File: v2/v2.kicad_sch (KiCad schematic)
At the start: 63 parts, among them SW1 SW_Push, SW10 SW_Push, SW11 SW_Push, SW12 SW_Push, SW13 SW_Push, SW14 SW_Push, SW15 SW_Push, SW16 SW_Push, SW17 SW_Push, SW18 SW_Push, SW19 SW_Push, SW2 SW_Push, SW20 SW_Push, SW21 SW_Push, SW22 SW_Push, SW23 SW_Push, SW24 SW_Push, SW25 SW_Push, SW26 SW_Push, SW27 SW_Push, SW28 SW_Push, SW29 SW_Push, SW3 SW_Push, SW30 SW_Push, SW31 SW_Push, SW4 SW_Push, SW5 SW_Push, SW6 SW_Push, SW7 SW_Push, SW8 SW_Push, SW9 SW_Push, U1 Pico

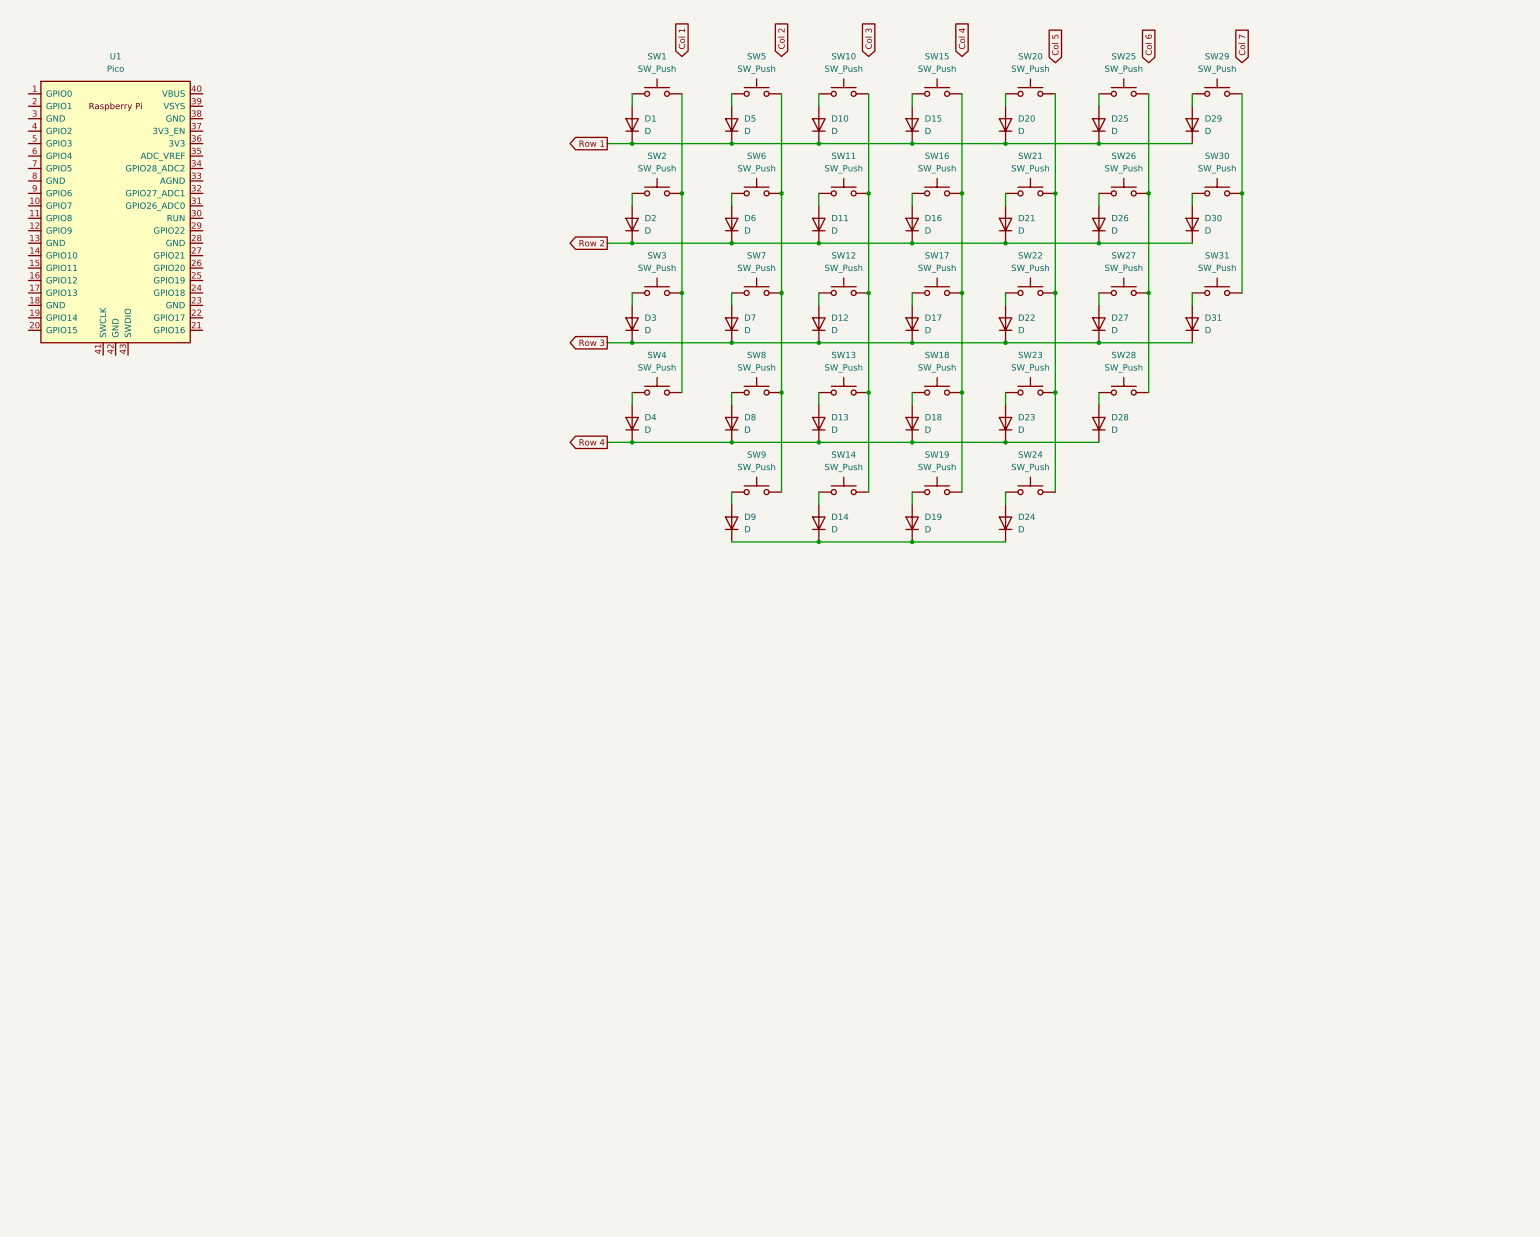
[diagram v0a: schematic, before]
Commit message: get the right footprints finally
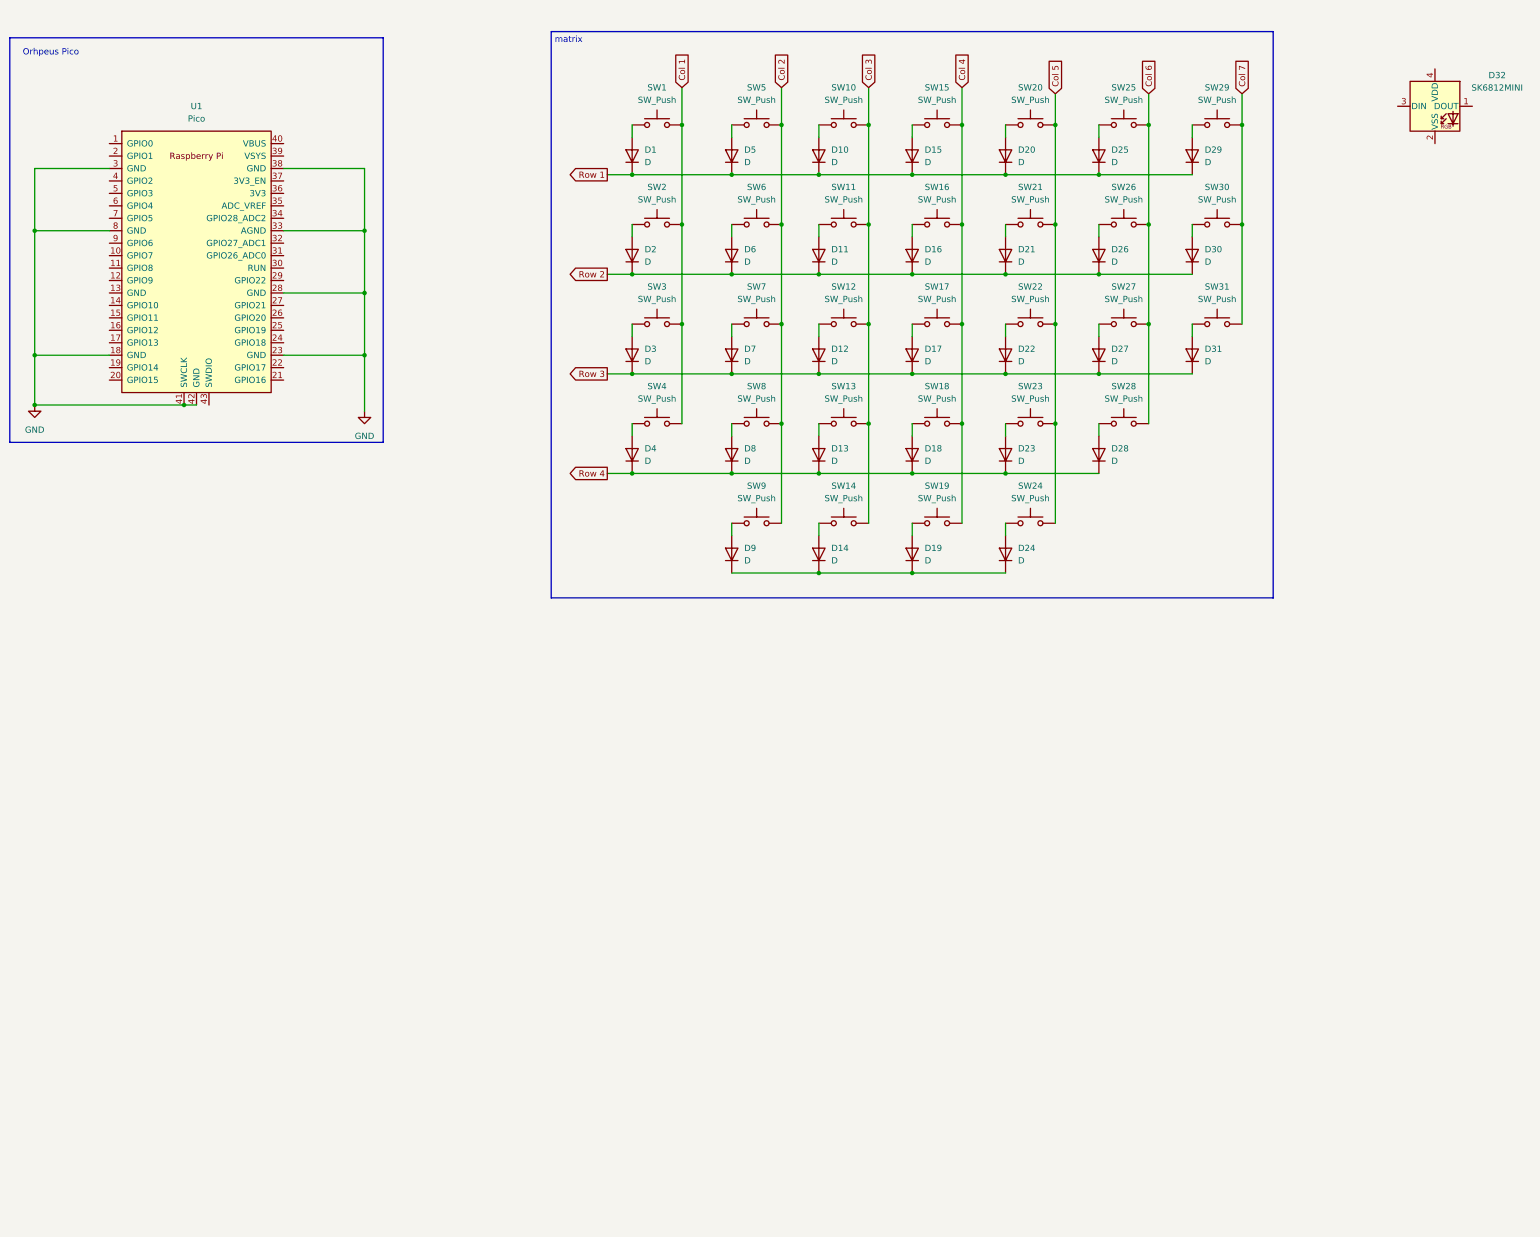
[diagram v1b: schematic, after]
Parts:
- added D32: SK6812MINI, reversible-kicad-footprints:MX-1U-SK6812Mini-E, symbol LED:SK6812MINI
- SW1, SW10, SW11, SW12, SW13, SW14, SW15, SW16, SW17, SW18, SW19, SW2, SW20, SW21, SW22, SW23, SW24, SW25, SW26, SW27, SW28, SW29, SW3, SW30, SW31, SW4, SW5, SW6, SW7, SW8, SW9: footprint (none) -> reversible-kicad-footprints:MX-1U-Hotswap
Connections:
- net Col 1: now also SW1.2, SW2.2, SW3.2, SW4.2
- net Col 2: now also SW5.2, SW6.2, SW7.2, SW8.2, SW9.2
- net Col 3: now also SW10.2, SW11.2, SW12.2, SW13.2, SW14.2
- net Col 4: now also SW15.2, SW16.2, SW17.2, SW18.2, SW19.2
- net Col 5: now also SW20.2, SW21.2, SW22.2, SW23.2, SW24.2
- net Col 6: now also SW25.2, SW26.2, SW27.2, SW28.2
- net Col 7: now also SW29.2, SW30.2, SW31.2
- net GND: now reaches U1.18 (GND)
- net GND: now also U1.23 (GND), U1.28 (GND), U1.3 (GND), U1.33 (AGND), U1.38 (GND), U1.41 (SWCLK), U1.42 (GND), U1.8 (GND)
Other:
- note added: "Orhpeus Pico"
- note added: "matrix"
- moved on the sheet: D1, D10, D11, D12, D13, D14, D15, D16, D17, D18, D19, D2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

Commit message: started adding backlighting
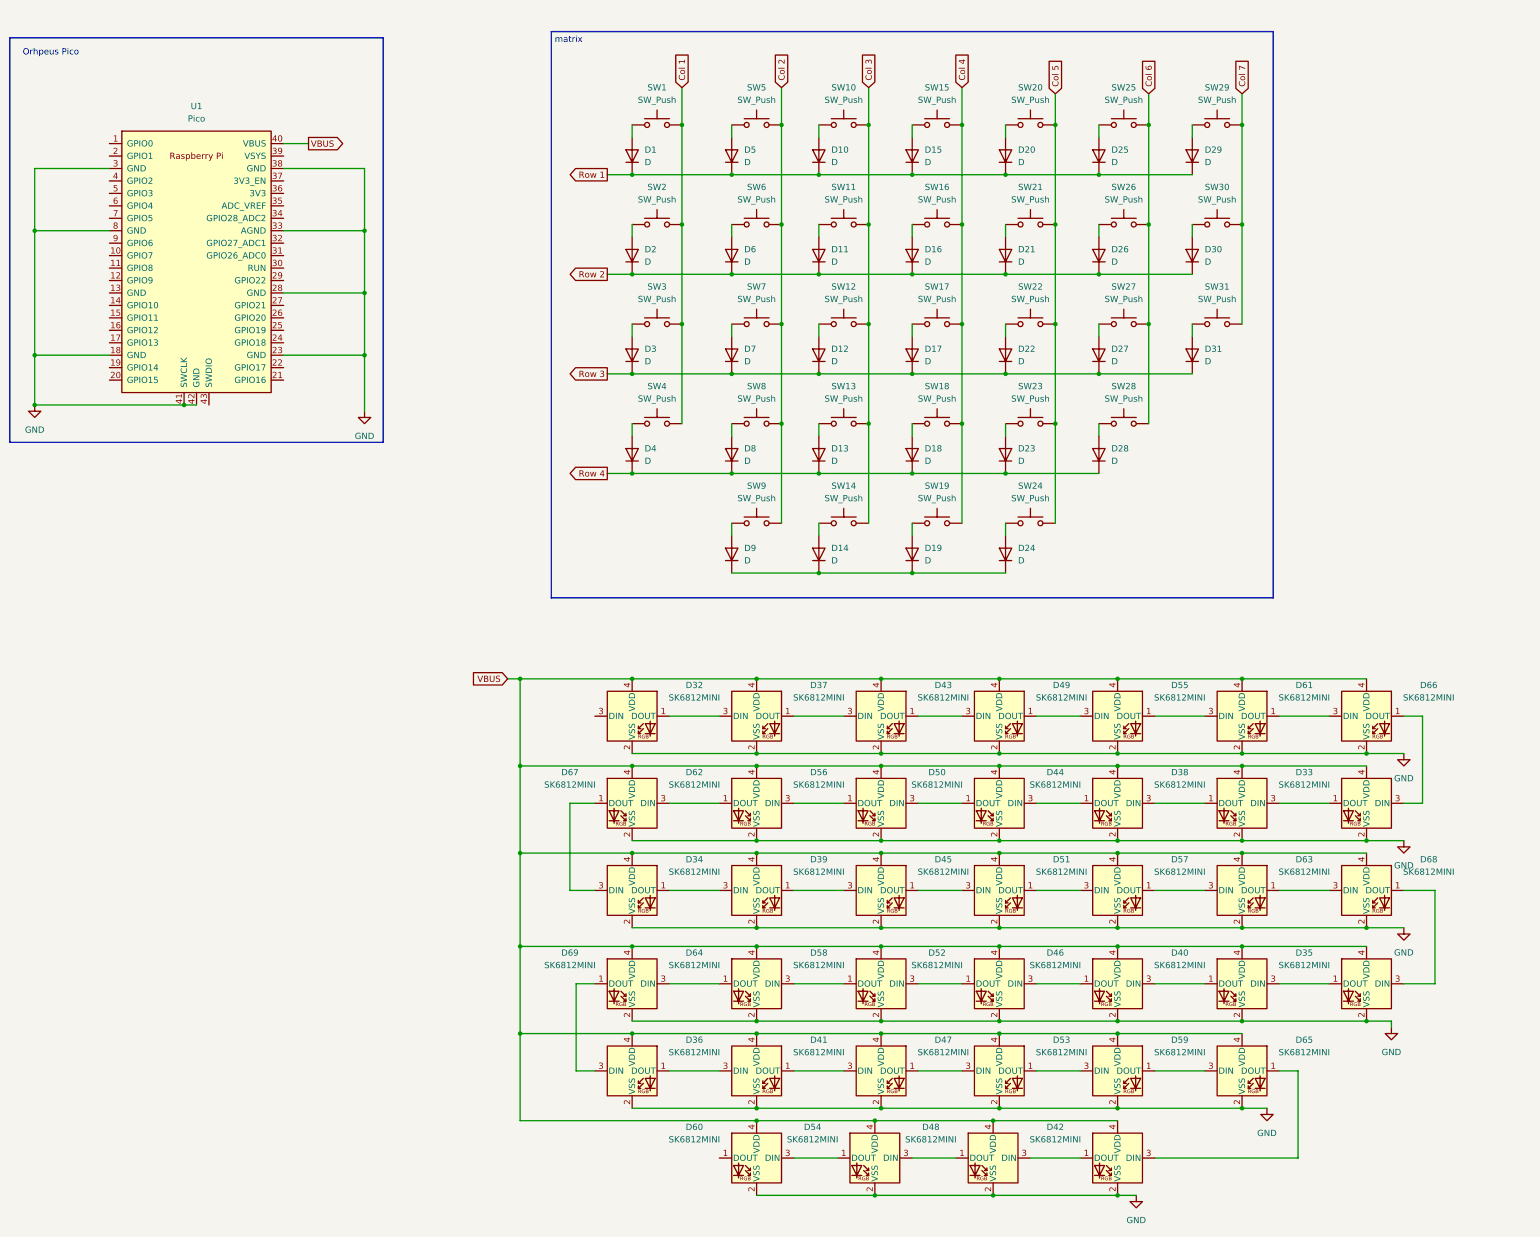
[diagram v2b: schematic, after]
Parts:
- added D33, D34, D35, D36, D37, D38, D39, D40, D41, D42, D43, D44, D45, D46, D47, D48, D49, D50, D51, D52, D53, D54, D55, D56, D57, D58, D59, D60, D61, D62, D63, D64, D65, D66, D67, D68, D69: SK6812MINI, reversible-kicad-footprints:MX-1U-SK6812Mini-E, symbol LED:SK6812MINI
- U1: footprint Module:RaspberryPi_Pico_SMD_HandSolder -> RPi_Pico:RPi_Pico_SMD_TH
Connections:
- net GND: now also D32.2 (VSS), D33.2 (VSS), D34.2 (VSS), D35.2 (VSS), D36.2 (VSS), D37.2 (VSS), D38.2 (VSS), D39.2 (VSS), D40.2 (VSS), D41.2 (VSS), D42.2 (VSS), D43.2 (VSS), D44.2 (VSS), D45.2 (VSS), D46.2 (VSS), D47.2 (VSS), D48.2 (VSS), D49.2 (VSS), D50.2 (VSS), D51.2 (VSS), D52.2 (VSS), D53.2 (VSS), D54.2 (VSS), D55.2 (VSS), D56.2 (VSS), D57.2 (VSS), D58.2 (VSS), D59.2 (VSS), D60.2 (VSS), D61.2 (VSS), D62.2 (VSS), D63.2 (VSS), D64.2 (VSS), D65.2 (VSS), D66.2 (VSS), D67.2 (VSS), D68.2 (VSS), D69.2 (VSS)
- net at D32.1 (DOUT): now also D37.3 (DIN)
- net VBUS: now reaches D32.4 (VDD)
- net VBUS: now also U1.40 (VBUS), D33.4 (VDD), D34.4 (VDD), D35.4 (VDD), D36.4 (VDD), D37.4 (VDD), D38.4 (VDD), D39.4 (VDD), D40.4 (VDD), D41.4 (VDD), D42.4 (VDD), D43.4 (VDD), D44.4 (VDD), D45.4 (VDD), D46.4 (VDD), D47.4 (VDD), D48.4 (VDD), D49.4 (VDD), D50.4 (VDD), D51.4 (VDD), D52.4 (VDD), D53.4 (VDD), D54.4 (VDD), D55.4 (VDD), D56.4 (VDD), D57.4 (VDD), D58.4 (VDD), D59.4 (VDD), D60.4 (VDD), D61.4 (VDD), D62.4 (VDD), D63.4 (VDD), D64.4 (VDD), D65.4 (VDD), D66.4 (VDD), D67.4 (VDD), D68.4 (VDD), D69.4 (VDD)
- new net: D37.1 (DOUT), D43.3 (DIN)
- new net: D63.1 (DOUT), D68.3 (DIN)
- new net: D57.1 (DOUT), D63.3 (DIN)
- new net: D54.1 (DOUT), D60.3 (DIN)
- new net: D45.1 (DOUT), D51.3 (DIN)
- new net: D39.1 (DOUT), D45.3 (DIN)
- new net: D46.1 (DOUT), D52.3 (DIN)
- new net: D40.1 (DOUT), D46.3 (DIN)
- new net: D36.3 (DIN), D69.1 (DOUT)
- new net: D64.1 (DOUT), D69.3 (DIN)
- new net: D34.1 (DOUT), D39.3 (DIN)
- new net: D34.3 (DIN), D67.1 (DOUT)
- new net: D35.1 (DOUT), D40.3 (DIN)
- new net: D35.3 (DIN), D68.1 (DOUT)
- new net: D42.3 (DIN), D65.1 (DOUT)
- new net: D59.1 (DOUT), D65.3 (DIN)
- new net: D62.1 (DOUT), D67.3 (DIN)
- new net: D56.1 (DOUT), D62.3 (DIN)
- new net: D58.1 (DOUT), D64.3 (DIN)
- new net: D48.1 (DOUT), D54.3 (DIN)
- new net: D50.1 (DOUT), D56.3 (DIN)
- new net: D44.1 (DOUT), D50.3 (DIN)
- new net: D51.1 (DOUT), D57.3 (DIN)
- new net: D42.1 (DOUT), D48.3 (DIN)
- new net: D49.1 (DOUT), D55.3 (DIN)
- new net: D43.1 (DOUT), D49.3 (DIN)
- new net: D53.1 (DOUT), D59.3 (DIN)
- new net: D47.1 (DOUT), D53.3 (DIN)
- new net: D61.1 (DOUT), D66.3 (DIN)
- new net: D55.1 (DOUT), D61.3 (DIN)
- new net: D33.1 (DOUT), D38.3 (DIN)
- new net: D33.3 (DIN), D66.1 (DOUT)
- new net: D38.1 (DOUT), D44.3 (DIN)
- new net: D41.1 (DOUT), D47.3 (DIN)
- new net: D36.1 (DOUT), D41.3 (DIN)
- new net: D52.1 (DOUT), D58.3 (DIN)
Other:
- moved on the sheet: D32
